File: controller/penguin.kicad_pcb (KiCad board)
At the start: 4 copper layers, 89.5 x 62.6 mm, 162 parts, among them IC1 HY2120-AB, J1 USB_C_CONN, J10 MTR_HEADER_2, J2 CAM_HEADER, J3 BATT_BALANCE_HEADER, J4 TOF_HEADER, J5 I2C_JUMPER, J6 I2C_JUMPER, J7 SERVO_CONN, J8 BATT_CONN, J9 MTR_HEADER_1, Q1 AO3400A, Q2 SI2393DS, Q3 2N7002, Q4 FS8205A, SW1 SW_Boot, SW2 SW_Reset, U1 ESP32-S3-WROOM-1U-N8R8, U10 TPS62143, U2 LP5907MFX-2.8, U3 LP5907MFX-1.2, U4 DRV8833PW, U5 MCP23017_ML, U6 TPS5405DR, U7 AMS1117-3.3, U8 DMP4065S-7, U9 LSM6DSL

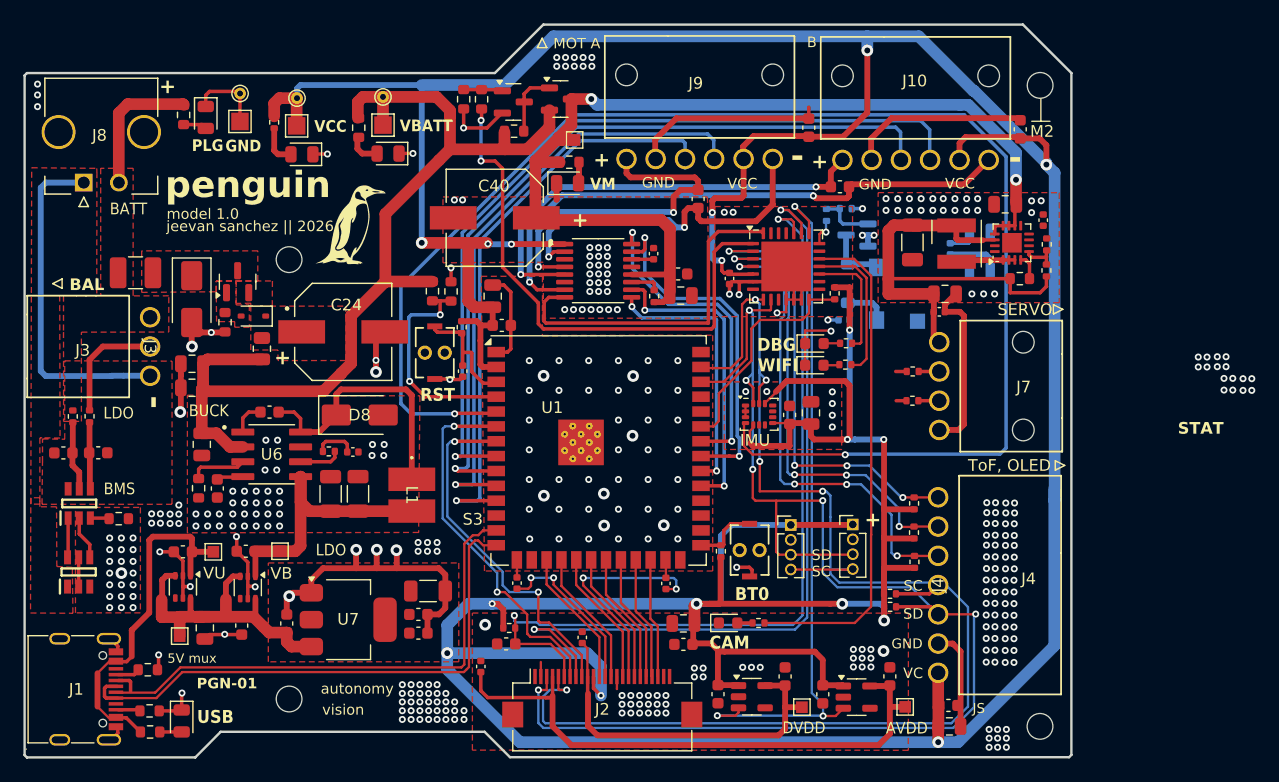
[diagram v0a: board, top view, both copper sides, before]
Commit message: added servo
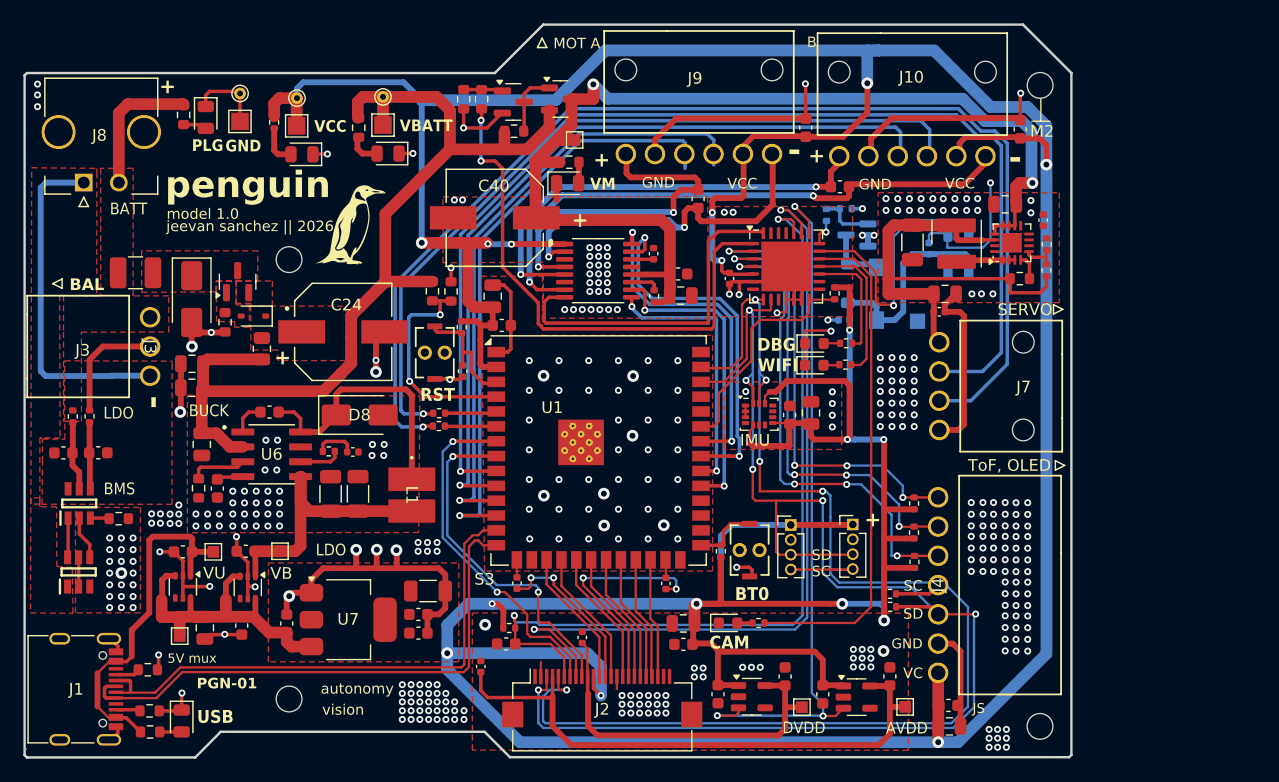
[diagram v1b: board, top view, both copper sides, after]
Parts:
- added G***: LOGO, LOGO, B.Cu at (118.1, 86.2)
- moved R31 40.8 mm to (131.1, 92.8), turned to 0 degrees
- moved R30 40.5 mm to (131.1, 91.7), turned to 0 degrees
- moved D4 1.84 mm to (175.5, 77.9)
- moved C52 1.82 mm to (173.0, 77.6)
- moved J9 0.43 mm to (147.1, 69.5)
- moved J10 0.42 mm to (165.3, 69.7)
- moved C20 0.26 mm to (162.4, 67.3)
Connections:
- C21 pad 2: +3V3 -> Net-(U4-VCP)
- R30 pad 1: Net-(J7-Pin_3) -> Net-(J7-Pin_2)
- R31 pad 1: Net-(J7-Pin_2) -> Net-(J7-Pin_3)
- U1 pad 10: ENC_A_PH1 -> ENC_B_PH2
- U1 pad 11: ENC_A_PH2 -> ENC_A_PH1
- U1 pad 12: unconnected-(U1-IO8-Pad12) -> ENC_A_PH2
- U1 pad 5: IMU_INT -> R_SERVO
- U1 pad 6: CAM_VSYNC -> L_SERVO
- U1 pad 7: CAM_HREF -> CAM_VSYNC
- U1 pad 8: ENC_B_PH1 -> CAM_HREF
- U1 pad 9: ENC_B_PH2 -> ENC_B_PH1
- U4 pad 11: +3V3 -> Net-(U4-VCP)
- U9 pad 4: IMU_INT -> unconnected-(U9-INT1-Pad4)
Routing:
- net IMU_INT: track 127.8 -> 0.00 mm, vias 10 -> 0
- net Net-(J7-Pin_3): track 1.78 -> 100.9 mm, vias 0 -> 1
- net Net-(J7-Pin_2): track 1.76 -> 95.7 mm, vias 0 -> 1
- net RGB_DATA: track 0.00 -> 23.6 mm, vias 0 -> 1
- net GND: track 181.7 -> 197.7 mm, vias 364 -> 378
- net +3V3: track 466.9 -> 473.2 mm
- net VMOT: track 85.2 -> 90.6 mm
- net R_SERVO: track 0.88 -> 4.64 mm
- net L_SERVO: track 0.95 -> 4.40 mm
- net Net-(U4-VCP): track 0.00 -> 2.56 mm
- net CAM_VSYNC: track 31.7 -> 30.0 mm
- net MOTB_IN1: track 30.0 -> 31.4 mm
- net ENC_A_PH2: track 50.8 -> 51.7 mm
- net MOTB_IN2: track 27.5 -> 28.4 mm
- net CAM_HREF: track 30.8 -> 29.9 mm
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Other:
- board text removed: "J4"
- board text removed: "STAT"

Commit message: finish hardware review
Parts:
- removed R39: R, Resistor_SMD:R_0402_1005Metric
- added D14: SERVO_V_LED, LED_SMD:LED_0603_1608Metric, F.Cu at (169.2, 85.7)
- added R40: 330, Resistor_SMD:R_0402_1005Metric, F.Cu at (169.4, 83.4)
- added TP13: VSERVO_TP_PAD, TestPoint:TestPoint_Pad_1.0x1.0mm, F.Cu at (171.6, 83.4)
- D10: footprint LED_SMD:LED_0805_2012Metric -> LED_SMD:LED_0603_1608Metric
- R16: value 180k -> 100k
- R19: value 1.2k -> 680
- R20: value 1k -> 680
- R21: value 330 -> 200; footprint Resistor_SMD:R_0402_1005Metric -> Resistor_SMD:R_0603_1608Metric
- R33: value R -> 10k
- moved R33 59.0 mm to (135.0, 113.8), turned to 0 degrees
- moved C11 2.10 mm to (134.5, 115.4)
- moved R21 0.46 mm to (116.8, 67.2)
- moved TP5 0.15 mm to (118.9, 67.0)
- moved TP6 0.15 mm to (118.9, 64.6)
- moved D12 0.15 mm to (119.3, 69.4)
- moved D10 0.15 mm to (142.2, 72.0)
- turned R16 to -90 degrees
- turned R20 to 180 degrees
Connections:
- J2 pad 1: unconnected-(J2-Pin_1-Pad1) -> Net-(J2-Pin_1)
- R16 pad 1: GND -> Net-(U6-ROSC)
- R16 pad 2: Net-(U6-ROSC) -> GND
- R20 pad 1: 5V_USB -> Net-(D11-A)
- R20 pad 2: Net-(D11-A) -> 5V_USB
- R33 pad 1: Net-(U10-FB) -> GND
- R33 pad 2: VSERVO -> Net-(J2-Pin_1)
- U10 pad 5: Net-(U10-FB) -> GND
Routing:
- net +3V3: track 473.2 -> 477.6 mm
- net Net-(J2-Pin_1): track 0.00 -> 4.05 mm
- net Net-(U10-FB): track 3.07 -> 0.00 mm
- net GND: track 197.7 -> 199.9 mm, vias 378 -> 360
- net ENC_A_PH2: track 51.7 -> 50.0 mm
- net VSERVO: track 39.6 -> 37.9 mm
- net CAM_AVDD: track 50.1 -> 48.4 mm
- net Net-(D14-A): track 0.00 -> 1.70 mm
- net ENC_A_PH1: track 53.1 -> 52.2 mm
- net Net-(D12-A): track 3.47 -> 2.68 mm
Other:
- board text added: "LIN"
- board text added: "RIN"
- board text added: "VS"
- board text added: "is 5V"
